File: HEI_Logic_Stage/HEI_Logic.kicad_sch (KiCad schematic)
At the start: 46 parts, among them J5 Tag-Connect, SW1 SW_Push, U6 STM32F334C8T6, U7 LM4132-Q1 SOT-2

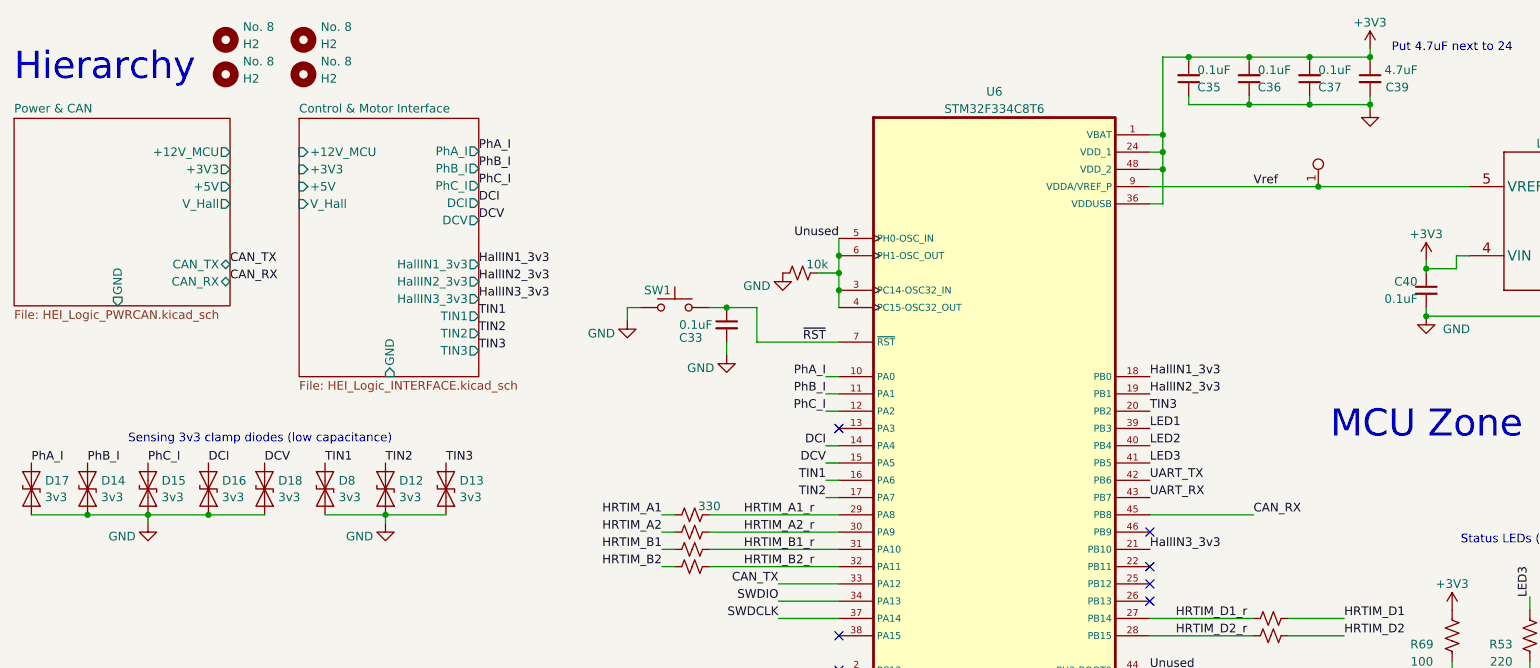
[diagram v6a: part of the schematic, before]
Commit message: fixed logic stage diff amp updates + sim
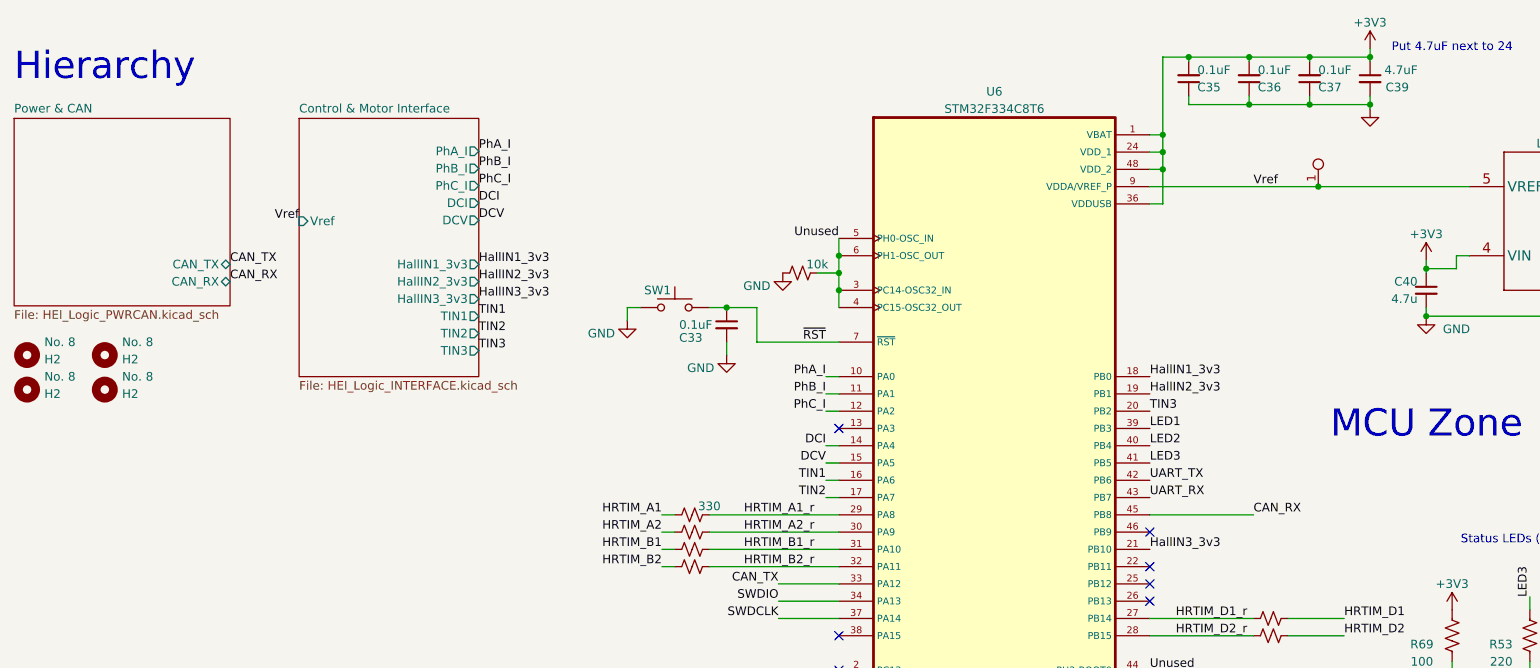
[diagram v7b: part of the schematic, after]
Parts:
- removed D12, D13, D14, D15, D16, D17, D18, D8: 3v3, Diode_SMD:D_SOD-923, symbol Diode:ESD9B3.3ST5G
- C40: value 0.1uF -> 4.7u
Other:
- sheet Control & Motor Interface ports: added Vref; removed +12V_MCU, +3V3, +5V, GND, V_Hall
- sheet Power & CAN ports: added none; removed +12V_MCU, +3V3, +5V, GND, V_Hall
- note removed: "Sensing 3v3 clamp diodes (low capacitance)"
- moved on the sheet: H2

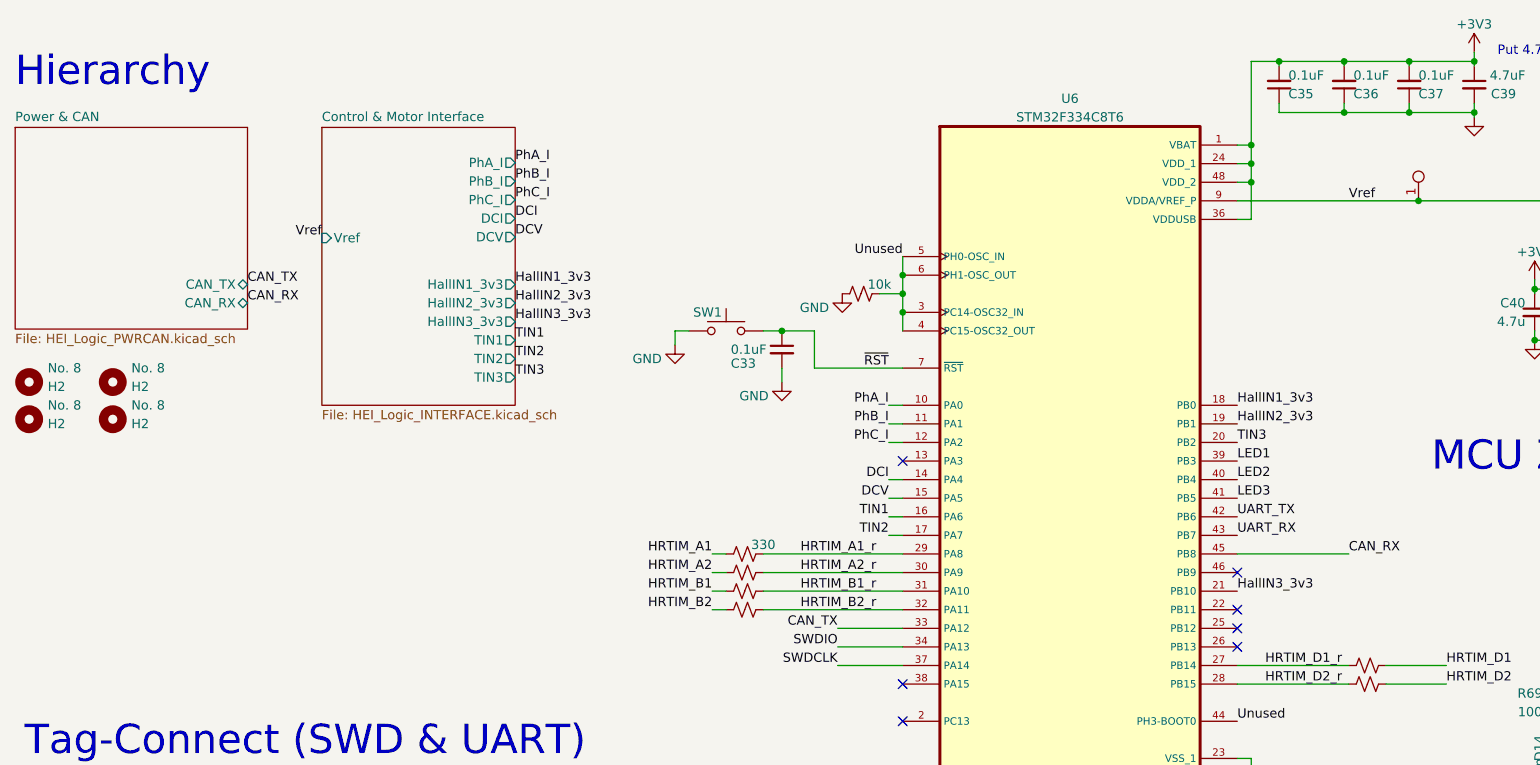
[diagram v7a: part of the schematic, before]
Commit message: vertical logic stage complete
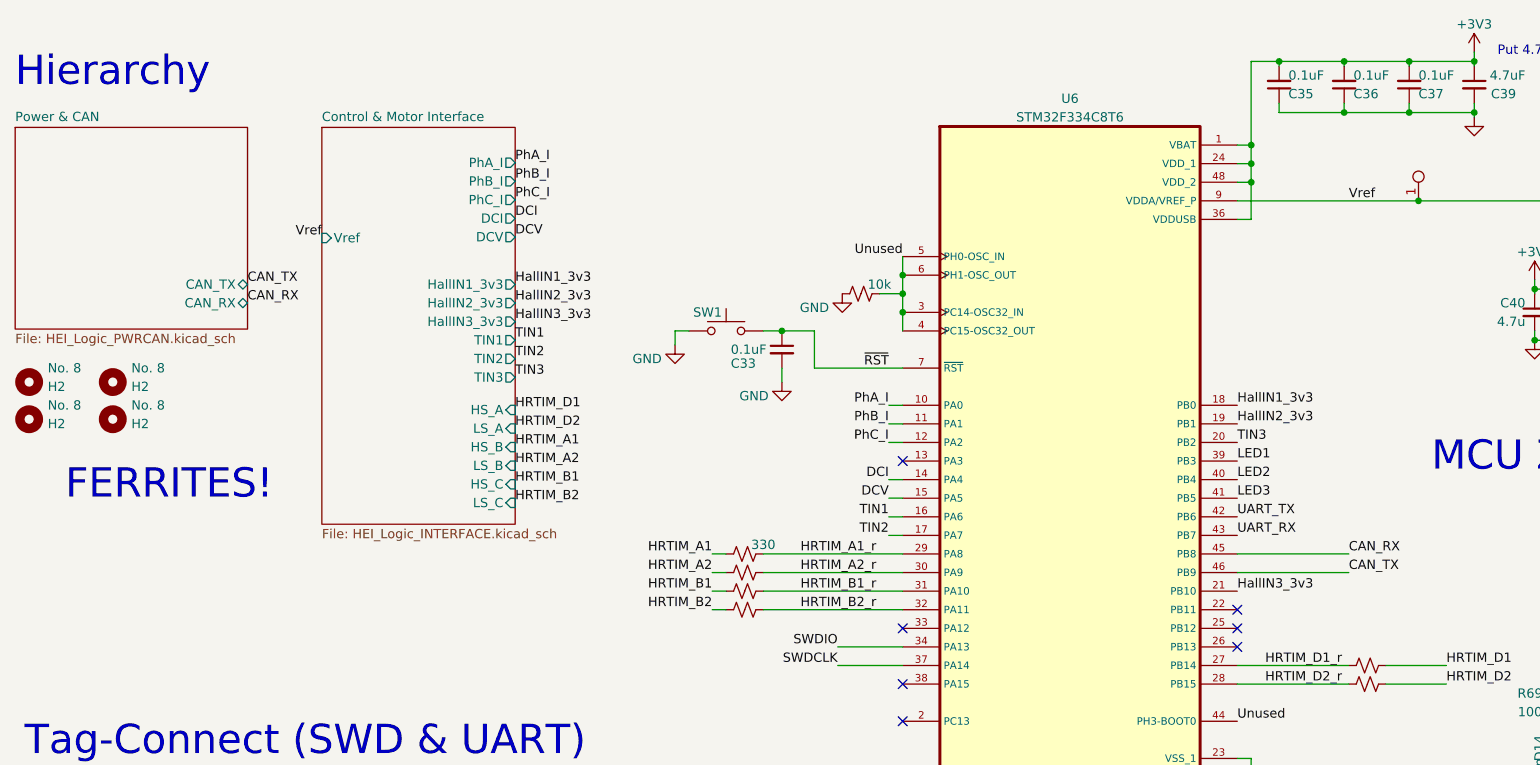
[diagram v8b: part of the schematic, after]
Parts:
- U6: footprint GTSR_KiCAD_Footprints:LQFP48-7x7mm -> HEI_Logic:LQFP48-7x7mm
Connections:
- net CAN_TX: now also U6.46 (PB9); no longer U6.33 (PA12)
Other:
- sheet Control & Motor Interface ports: added HS_A, HS_B, HS_C, LS_A, LS_B, LS_C; removed none
- note added: "FERRITES!"
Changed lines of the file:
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@@
 	)
 	(no_connect
+		(at 139.065 99.06)
+	)
+	(no_connect
 		(at 139.065 106.68)
 	)
@@
 		(at 39.37 132.08)
 	)
-	(no_connect
-		(at 184.785 91.44)
-	)
 	(wire
 		(pts
@@
 	(wire
 		(pts
+			(xy 184.785 91.44) (xy 200.025 91.44)
+		)
+		(stroke
+			(width 0)
+			(type default)
+		)
+	)
+	(wire
+		(pts
 			(xy 137.16 71.12) (xy 139.065 71.12)
 		)
@@
 	(wire
 		(pts
-			(xy 130.175 99.06) (xy 139.065 99.06)
-		)
-		(stroke
-			(width 0)
-			(type default)
-		)
-	)
-	(wire
-		(pts
 			(xy 37.465 135.255) (xy 38.735 135.255)
 		)
@@
 		)
 	)
+	(text "FERRITES!\n"
+		(exclude_from_sim no)
+		(at 24.638 81.788 0)
+		(effects
+			(font
+				(face "Rockwell")
+				(size 4 4)
+			)
+			(justify left bottom)
+		)
+	)
 	(text "MCU Zone"
 		(exclude_from_sim no)
@@
 		)
 	)
+	(label "HRTIM_A1"
+		(at 86.106 74.295 0)
+		(fields_autoplaced yes)
+		(effects
+			(font
+				(size 1.27 1.27)
+			)
+			(justify left bottom)
+		)
+	)
 	(label "PhB_I"
 		(at 137.16 71.12 180)
@@
 		)
 	)
+	(label "CAN_TX"
+		(at 200.025 91.44 0)
+		(fields_autoplaced yes)
+		(effects
+			(font
+				(size 1.27 1.27)
+			)
+			(justify left bottom)
+		)
+	)
+	(label "HRTIM_B2"
+		(at 86.106 81.915 0)
+		(fields_autoplaced yes)
+		(effects
+			(font
+				(size 1.27 1.27)
+			)
+			(justify left bottom)
+		)
+	)
 	(label "PhB_I"
 		(at 86.106 37.973 0)
@@
 		)
 	)
+	(label "HRTIM_B1"
+		(at 86.106 79.375 0)
+		(fields_autoplaced yes)
+		(effects
+			(font
+				(size 1.27 1.27)
+			)
+			(justify left bottom)
+		)
+	)
 	(label "CAN_RX"
 		(at 49.53 54.61 0)
@@
 		)
 	)
-	(label "CAN_TX"
-		(at 130.175 99.06 180)
+	(label "HRTIM_A2"
+		(at 86.106 76.835 0)
 		(fields_autoplaced yes)
 		(effects
@@
 				(size 1.27 1.27)
 			)
-			(justify right bottom)
+			(justify left bottom)
 		)
 	)
@@
 		)
 	)
+	(label "HRTIM_D2"
+		(at 86.106 71.755 0)
+		(fields_autoplaced yes)
+		(effects
+			(font
+				(size 1.27 1.27)
+			)
+			(justify left bottom)
+		)
+	)
 	(label "LED1"
 		(at 184.785 76.2 0)
@@
 	(label "Vref"
 		(at 59.69 45.72 180)
+		(fields_autoplaced yes)
 		(effects
 			(font
@@
 		)
 	)
+	(label "HRTIM_D1"
+		(at 86.106 69.215 0)
+		(fields_autoplaced yes)
+		(effects
+			(font
+				(size 1.27 1.27)
+			)
+			(justify left bottom)
+		)
+	)
 	(label "HRTIM_D1_r"
 		(at 188.595 104.14 0)
@@
 			)
 		)
-		(property "Footprint" "GTSR_KiCAD_Footprints:LQFP48-7x7mm"
+		(property "Footprint" "HEI_Logic:LQFP48-7x7mm"
 			(at 162.56 27.94 0)
 			(effects
@@
 	(sheet
 		(at 59.69 30.607)
-		(size 26.416 37.973)
+		(size 26.416 54.229)
 		(fields_autoplaced yes)
 		(stroke
@@
 		)
 		(property "Sheetfile" "HEI_Logic_INTERFACE.kicad_sch"
-			(at 59.69 69.1646 0)
+			(at 59.69 85.4206 0)
 			(effects
 				(font
@@
 			)
 		)
+		(pin "HS_A" input
+			(at 86.106 69.215 0)
+			(effects
+				(font
+					(size 1.27 1.27)
+				)
+				(justify right)
+			)
+		)
+		(pin "HS_C" input
+			(at 86.106 79.375 0)
+			(effects
+				(font
+					(size 1.27 1.27)
+				)
+				(justify right)
+			)
+		)
+		(pin "HS_B" input
+			(at 86.106 74.295 0)
+			(effects
+				(font
+					(size 1.27 1.27)
+				)
+				(justify right)
+			)
+		)
+		(pin "LS_B" input
+			(at 86.106 76.835 0)
+			(effects
+				(font
+					(size 1.27 1.27)
+				)
+				(justify right)
+			)
+		)
+		(pin "LS_C" input
+			(at 86.106 81.915 0)
+			(effects
+				(font
+					(size 1.27 1.27)
+				)
+				(justify right)
+			)
+		)
+		(pin "LS_A" input
+			(at 86.106 71.755 0)
+			(effects
+				(font
+					(size 1.27 1.27)
+				)
+				(justify right)
+			)
+		)
